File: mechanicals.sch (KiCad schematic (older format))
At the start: 20 parts

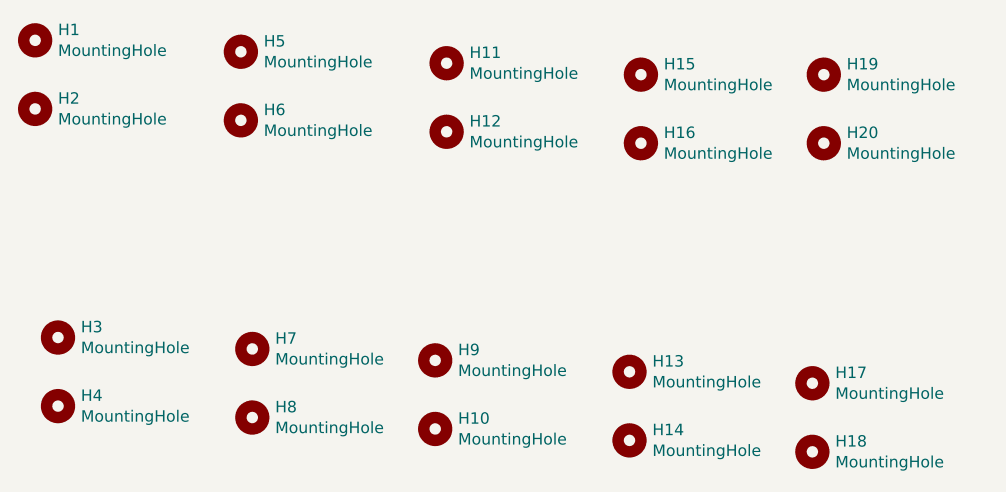
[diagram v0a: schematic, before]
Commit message: Schematic is almost finished. The MCLR circuit needs completing, the hour/minute inputs also need their input protection.
After that, I might have one of the guys from work review it. But, who knows.
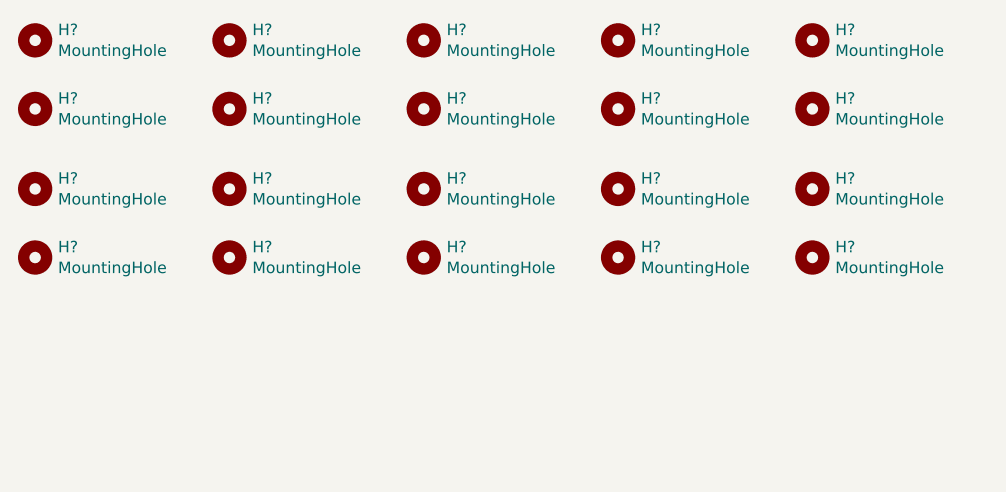
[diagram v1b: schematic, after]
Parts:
- renumbered H1 to H?, H2 to H?, H11 to H?, H12 to H?, H15 to H?, H16 to H?, H19 to H?, H20 to H?, H9 to H?, H10 to H?, H13 to H?, H14 to H?, H3 to H?, H4 to H?, H7 to H?, H8 to H?, H5 to H?, H6 to H?, H18 to H?, H17 to H?
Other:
- moved on the sheet: H?
